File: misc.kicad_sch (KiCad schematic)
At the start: 119 parts, among them CN2 Expansion, CN3 Cartridge, CN5 1P, CN504 AV Out, CN6 1P, IC513 MC34063AM, IC514 L7805, IC701 PIC16F630/18324, IC901 TL974, J1 Barrel_Jack, J701 0, U1 TPS564257DRLR, U4 L7805

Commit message: First draft "full" layout, bar a few passives.
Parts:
- added Q1: MMBT3904, Package_TO_SOT_SMD:SOT-23, symbol Transistor_BJT:MMBT3904
- added R2: 10K, Resistor_SMD:R_0805_2012Metric, symbol Device:R
- added R2: 4.7K, Resistor_SMD:R_0805_2012Metric, symbol Device:R
- added TP1: +9V, Connector_PinHeader_2.54mm:PinHeader_1x01_P2.54mm_Vertical, symbol Connector:TestPoint_Alt
- C1, C6, C9: footprint Capacitor_SMD:C_0603_1608Metric -> Capacitor_SMD:C_0805_2012Metric
- CE517, CE518: now in the parts list
- R1, R2: footprint Resistor_SMD:R_0603_1608Metric -> Resistor_SMD:R_0805_2012Metric
- R3, R4, R5: footprint Resistor_SMD:R_0603_1608Metric -> Capacitor_SMD:C_0805_2012Metric
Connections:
- net +5V: no longer C1.1, C1.1, C2.1, C3.1, C4.1, C5.1, C584.1, C6.1, C701.1, CE17.1, CE18.1, CE19.1, CE27.1, CE28.1, CE517.1, CE518.1, CN2.a26 (Pin_a26), CN2.b26 (Pin_b26), D1.1 (K), EM15.3, EM25.3, IC701.1 (VDD), L1.2, L507.1, L6.2, NF502.3, NT1.1, NT1.2, NT2.1, NT2.2, NT3.1, NT4.2, OSC1.14 (Vcc), R3.1, R48.1, R5.2, R50.1, R51.1, R52.1, R553.1, R601.1, R65.1, U4.3 (OUT)
- net +9V: now also TP1.1
- net GND: now also C7.2, C8.2, C9.2, J1.2, R1.2, S2.1 (A), Q1.2 (E), R2.2
- net at C7.1, C8.1, C9.1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: now also R2.1
- net at U1.5 (EN): now also R1.1, R2.2, Q1.3 (C); no longer S2.2 (B)
- new net: Q1.1 (B), R2.1, R2.2, S2.2 (B)
- new net AVCC: NT2.2
- new net VCC1: C1.1, C1.1, C2.1, C3.1, C4.1, C5.1, C584.1, C6.1, C701.1, CE17.1, CE18.1, CE19.1, CE27.1, CE28.1, CE517.1, CE518.1, CN2.a26 (Pin_a26), CN2.b26 (Pin_b26), D1.1 (K), EM15.3, EM25.3, IC701.1 (VDD), L1.2, L507.1, L6.2, NF502.3, NT1.1, NT2.1, NT3.1, NT4.2, OSC1.14 (Vcc), R3.1, R5.2, R553.1, R601.1, R65.1, U4.3 (OUT)
- new net VVCC: NT1.2, R48.1, R50.1, R51.1, R52.1
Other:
- moved on the sheet: C1, C2, C3, C4, C5, C6, C7, C8, C9, J1, L1, NT1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

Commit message: Place remaining passives.
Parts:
- removed NT3: ~, NetTie:NetTie-2_SMD_Pad0.5mm, symbol Device:NetTie_2
- added NT6: ~, NetTie:NetTie-2_SMD_Pad0.5mm, symbol Device:NetTie_2
- C44: now left out of the parts list
- D1: footprint (none) -> Diode_THT:D_T-1_P5.08mm_Horizontal
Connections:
- net +5V is gone; now on net VCC1: CN3.a2 (Pin_a2), CN3.a31 (Pin_a31), IC514.1 (IN), R556.1
- net GND: now also NT6.1
- new net GNDA2: NT6.2
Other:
- note removed: "MD VCC is used as +5V on 32X"

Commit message: Some power routing.
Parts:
- added C45: 22nF, Capacitor_SMD:C_0805_2012Metric, symbol Device:C
- added CE508, CE509: 47uF, Capacitor_THT:CP_Radial_D5.0mm_P2.50mm, symbol Device:C_Polarized
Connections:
- net GND: now also C45.2, CE508.2, CE509.2
- net VCC1: now also C45.1, CE508.1, CE509.1
- net ~{PWR_EN}: now reaches Q1.1 (B), R2.1, R2.2, S2.2 (B)
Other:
- moved on the sheet: S2

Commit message: More power routing, ground planes.
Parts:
- removed NT4, NT6: ~, NetTie:NetTie-2_SMD_Pad0.5mm, symbol Device:NetTie_2
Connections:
- net AVCC2 is gone; now on net AVCC: CE519.1, L6.1
- net VVCC is gone; now on net AVCC: NT1.2, R48.1, R50.1, R51.1, R52.1
- net GND: no longer NT5.2
- new net GNDA: NT5.2
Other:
- moved on the sheet: NT2

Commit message: Fill zones, DRC fixes.
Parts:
- removed J701: 0, Resistor_SMD:R_0805_2012Metric, symbol Device:R
- added J2: EXT, Neptune:EXT_Breakout, symbol Connector_Generic:Conn_01x09
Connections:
- net GND: now also J2.9 (Pin_9); no longer CN504.10 (Pin_10)
- net GNDA: now also CN504.10 (Pin_10)
- net VCC1: now also J2.1 (Pin_1)
- new net PC0: J2.2 (Pin_2)
- new net PC1: J2.3 (Pin_3)
- new net PC2: J2.4 (Pin_4)
- new net PC3: J2.5 (Pin_5)
- new net PC4: J2.6 (Pin_6)
- new net PC5: J2.7 (Pin_7)
- new net PC6: J2.8 (Pin_8)
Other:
- note added: "Link if no IC701"
- note removed: "Close if no IC701"

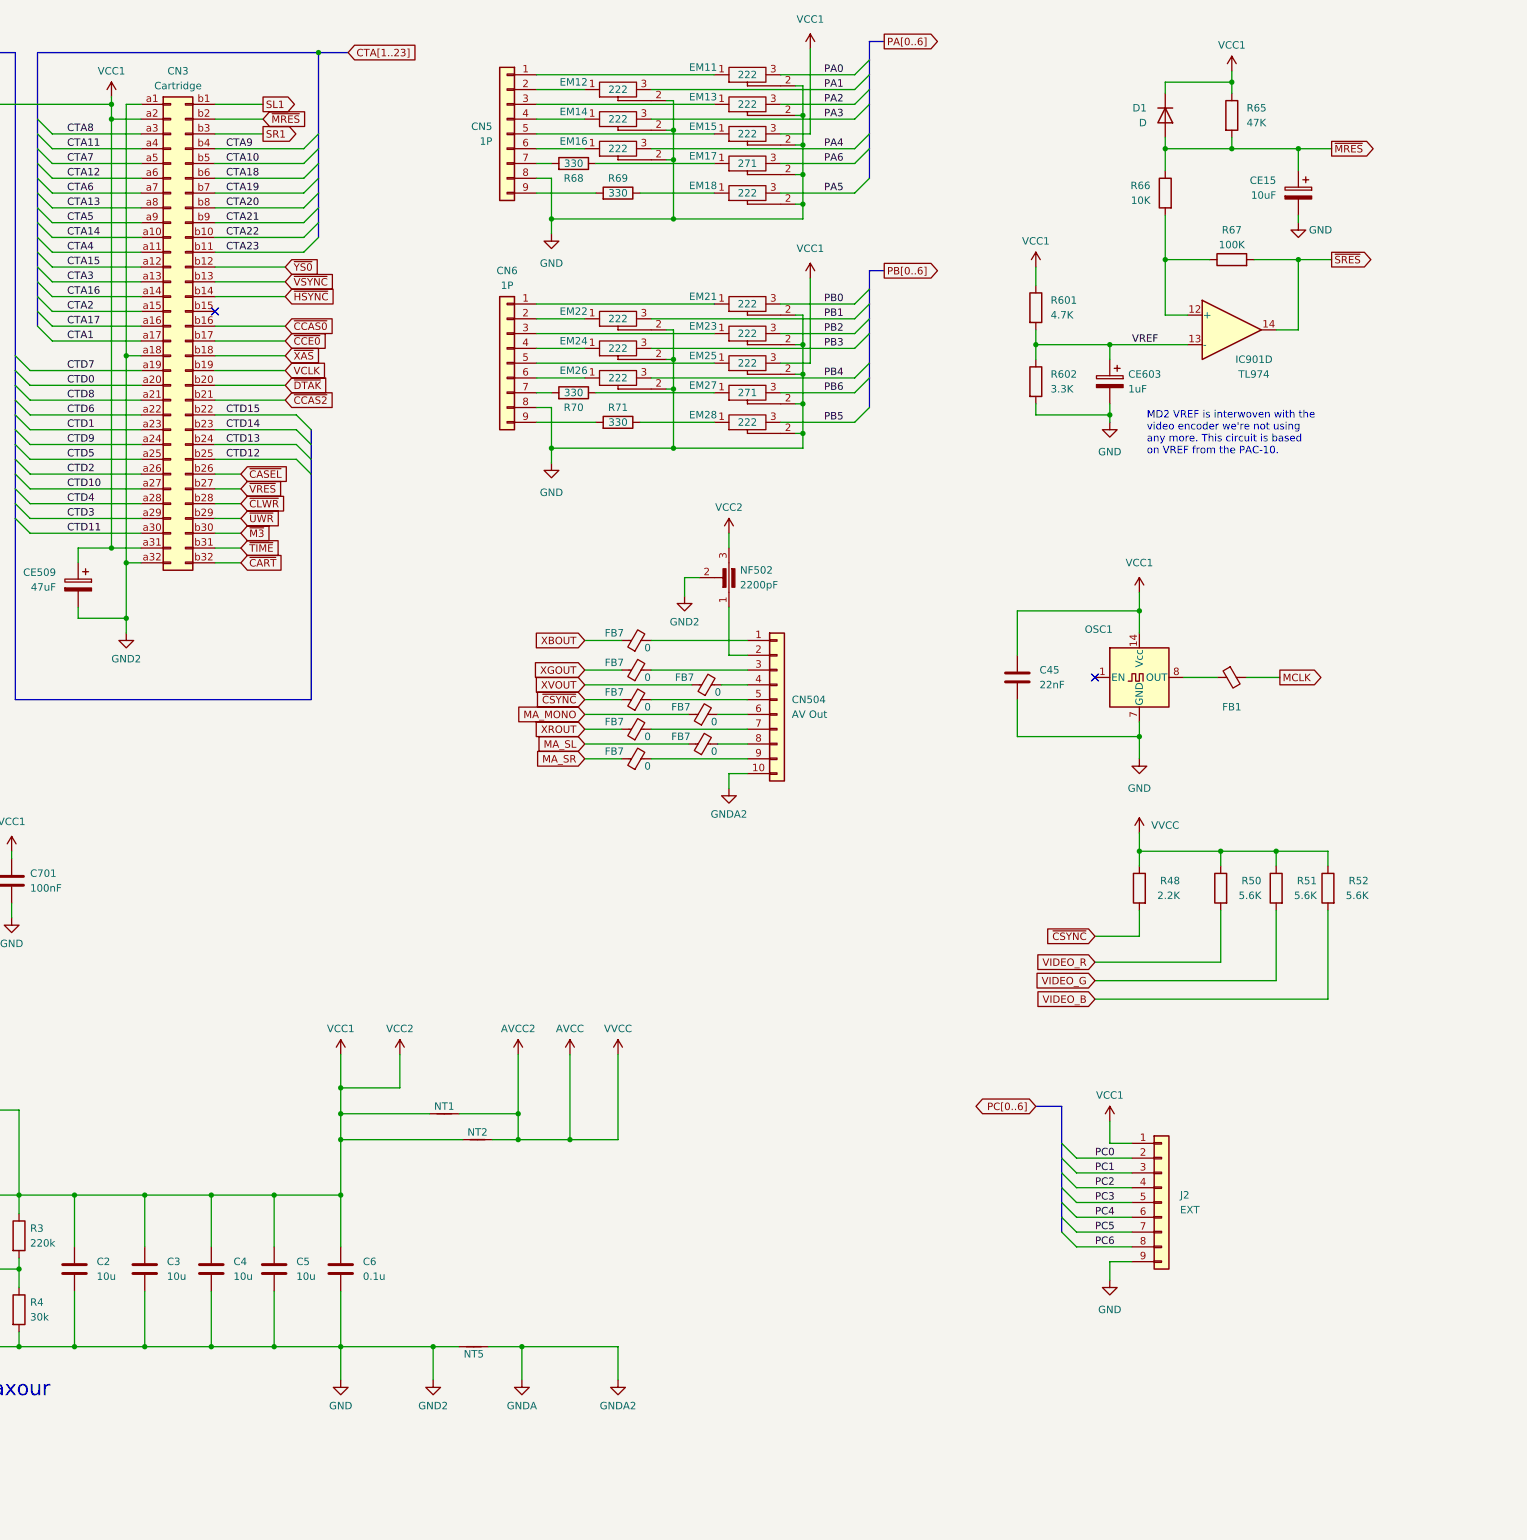
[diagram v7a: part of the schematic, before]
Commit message: SMS compatibility fixes.
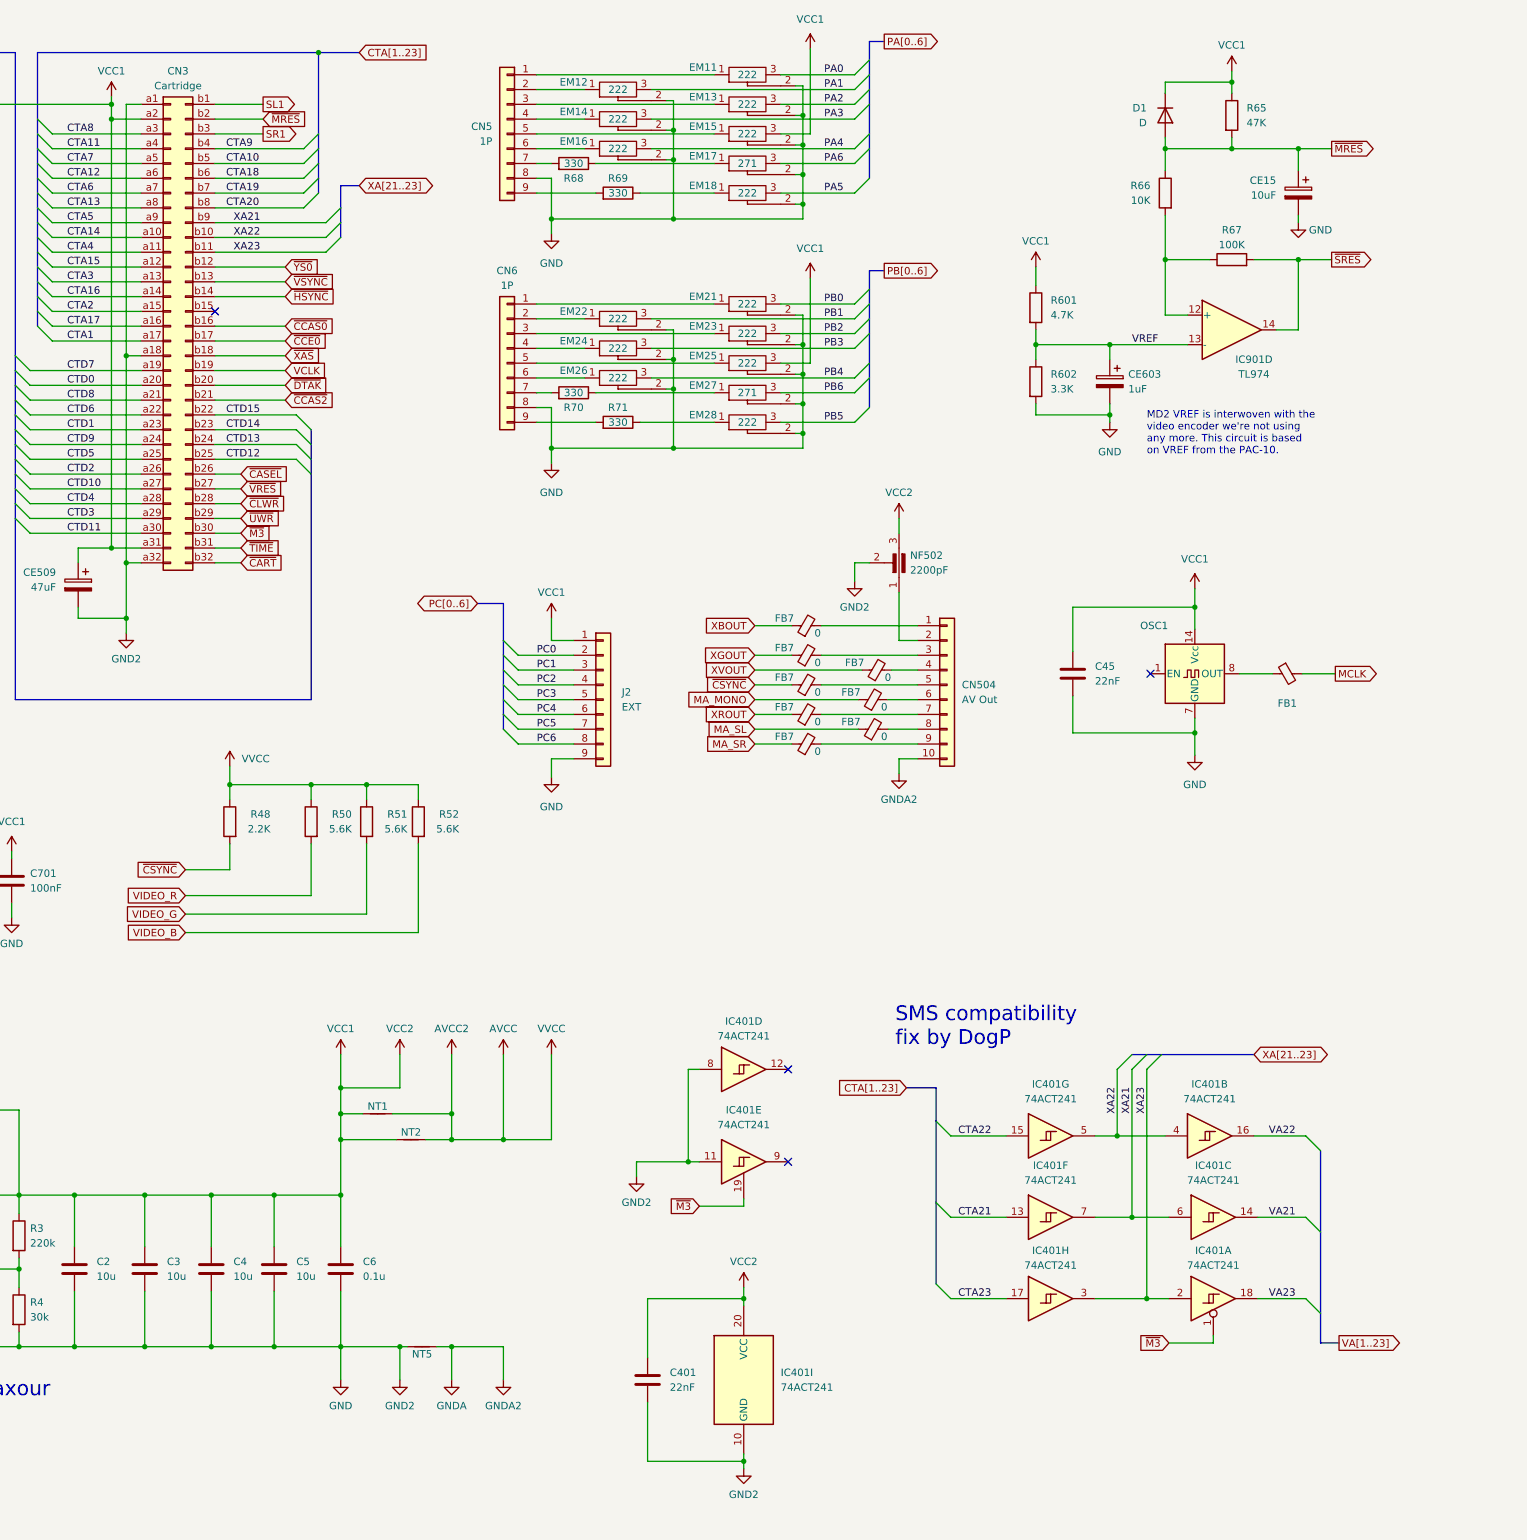
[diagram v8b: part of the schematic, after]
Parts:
- added C401: 22nF, Capacitor_SMD:C_0805_2012Metric, symbol Device:C
- added IC401: 74ACT241, Package_SO:TSSOP-20_4.4x6.5mm_P0.65mm, symbol 74xx:74LS241_Split
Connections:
- net CTA21: now also IC401.13; no longer CN3.b9 (Pin_b9)
- net CTA22: now also IC401.15; no longer CN3.b10 (Pin_b10)
- net CTA23: now also IC401.17; no longer CN3.b11 (Pin_b11)
- net GND: now also C401.2, IC401.10 (GND), IC401.11, IC401.8
- net VCC1: now also C401.1, IC401.20 (VCC)
- net ~{M3}: now also IC401.1, IC401.19
- new net VA21: IC401.14
- new net VA22: IC401.16
- new net VA23: IC401.18
- new net XA21: CN3.b9 (Pin_b9), IC401.6, IC401.7
- new net XA22: CN3.b10 (Pin_b10), IC401.4, IC401.5
- new net XA23: CN3.b11 (Pin_b11), IC401.2, IC401.3
- no-connect marks 7 -> 9
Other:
- note added: "SMS compatibility fix by DogP"
- moved on the sheet: C45, CN504, FB1, FB7, J2, NF502, NT1, NT2, NT5, OSC1, R48, R50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
